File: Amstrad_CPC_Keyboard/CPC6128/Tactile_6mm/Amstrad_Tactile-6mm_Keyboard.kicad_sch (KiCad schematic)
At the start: 87 parts, among them J1 CP002, J3 CP001, J4 CP003, SW1 DEL (79), SW10 FOUR (56), SW11 THREE (57), SW12 E (58), SW13 W (59), SW14 S (60), SW15 D (61), SW16 C (62), SW17 X (63), SW18 SIX (48), SW19 FIVE (49), SW2 ONE (64), SW20 R (50), SW21 T (51), SW22 G (52), SW23 F (53), SW24 B (54), SW25 V (55), SW26 EIGHT (40), SW27 ZERO (32), SW28 ^CARAT^ (24), SW29 SEVEN (41), SW3 TWO (65), SW30 NINE (33), SW31 -MINUS- (25), SW32 U (42), SW33 O (34), SW34 @AT@ (26), SW35 Y (43), SW36 I (35), SW37 P (27), SW38 H (44), SW39 L (36), SW4 ESC (66), SW40 ;SEMI_COLON; (28), SW41 J (45), SW42 K (37), SW43 :COLON: (29), SW44 N (46), SW45 M (38), SW46 /FORWSLASH/ (30), SW47 SPACE (47), SW48 ,COMMA, (39), SW49 .DOT. (31), SW5 Q (67), SW50 CLR (16), SW51 LEFT (08), SW52 UP (00), SW53 [ (17), SW54 COPY (09), SW55 RIGHT (01), SW56 ENTER (18), SW57 ƒ7 (10), SW58 DOWN (02), SW59 ] (19), SW6 TAB (68), SW60 ƒ8 (11), SW61 ƒ9 (03), SW62 ƒ4 (20), SW63 ƒ5 (12), SW64 ƒ6 (04), SW65 LH_SHIFT (21), SW66 ƒ1 (13), SW67 ƒ3 (05), SW68 \BACKSLASH\ (22), SW69 ƒ2 (14), SW7 A (69), SW70 ENTER (06), SW71 CTRL (23), SW72 ƒ0 (15), SW73 .DOT. (07), SW74 RH_SHIFT (21), SW75 SW_SPDT, SW8 CAPS_LOCK (70), SW9 Z (71)

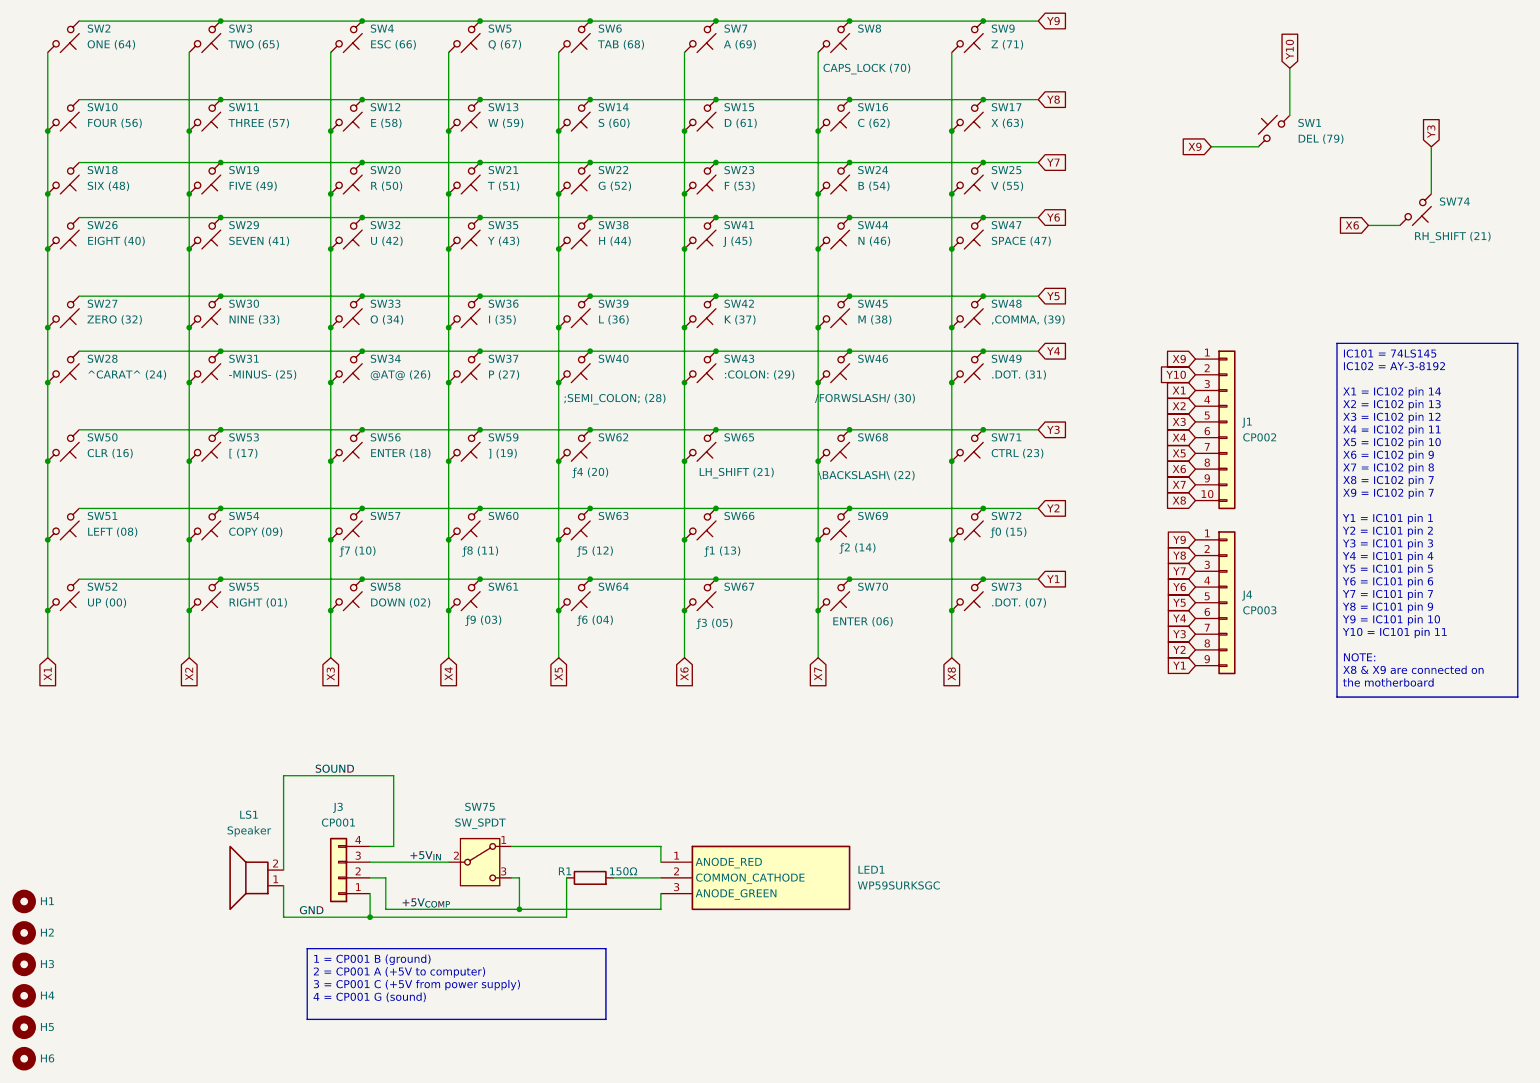
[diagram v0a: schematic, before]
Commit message: Added 6mm tactile design
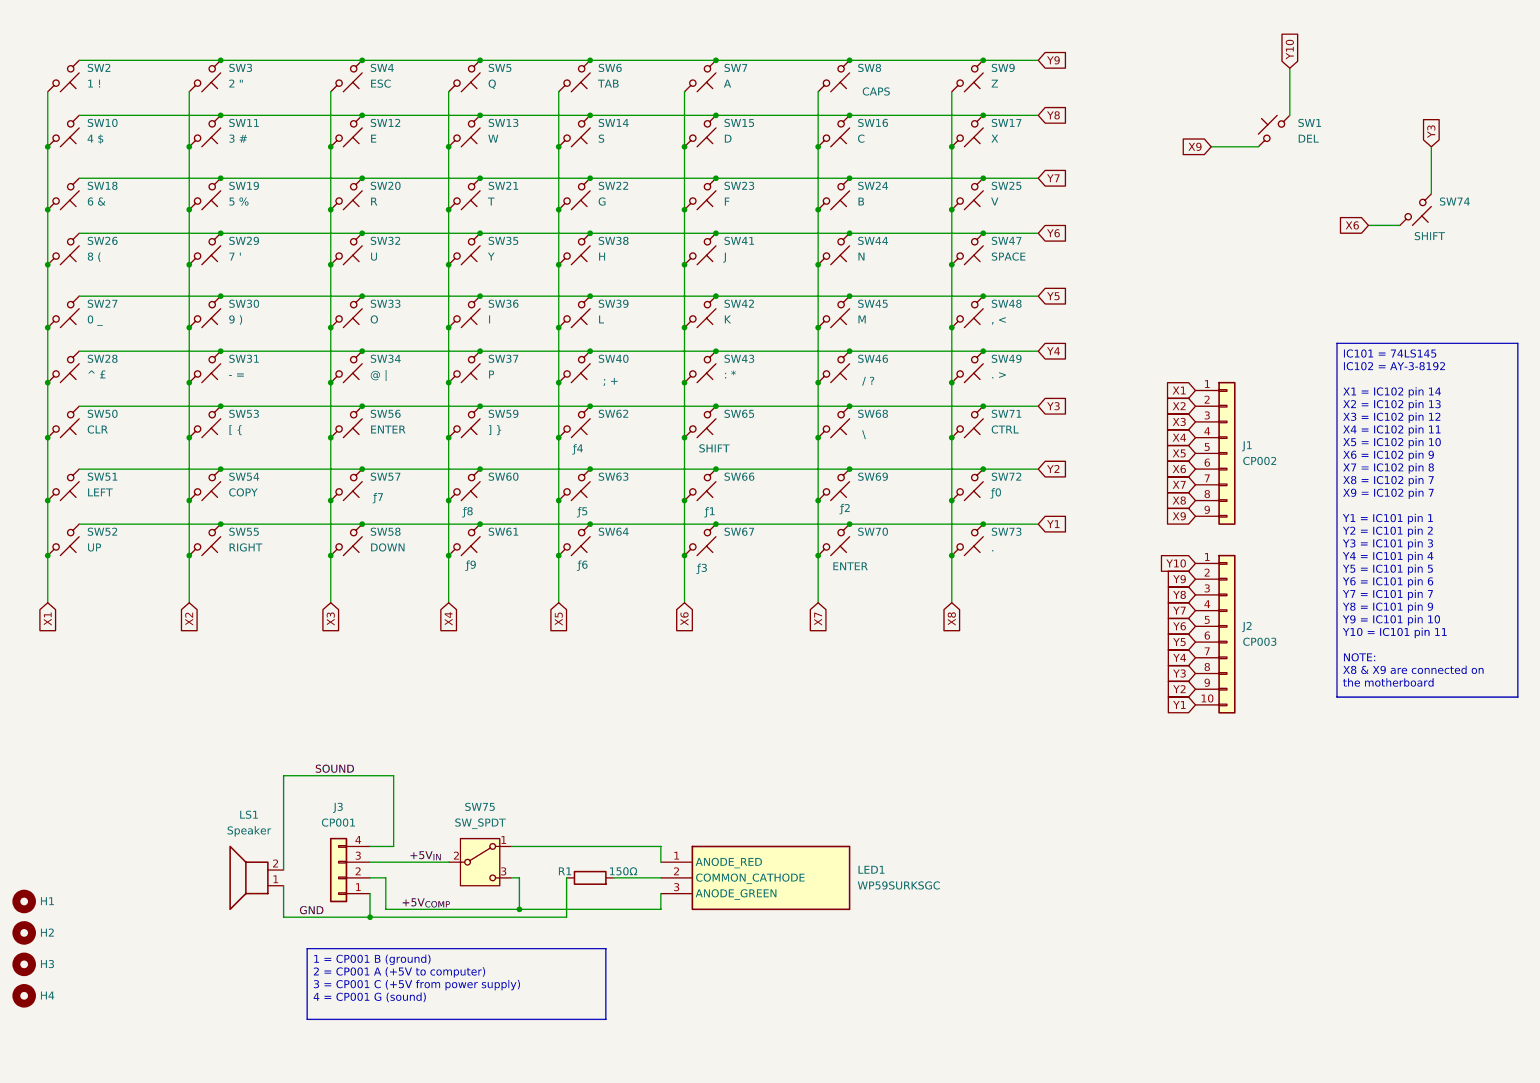
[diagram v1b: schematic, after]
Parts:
- removed H5, H6: MountingHole, MountingHole:MountingHole_3.2mm_M3, symbol Mechanical:MountingHole
- removed J1: CP002, Connector_PinHeader_2.54mm:PinHeader_1x10_P2.54mm_Vertical, symbol Connector_Generic:Conn_01x10
- removed J4: CP003, Connector_PinHeader_2.54mm:PinHeader_1x09_P2.54mm_Vertical, symbol Connector_Generic:Conn_01x09
- added J1: CP002, Connector_PinHeader_2.54mm:PinHeader_1x09_P2.54mm_Vertical, symbol Connector_Generic:Conn_01x09
- added J2: CP003, Connector_PinHeader_2.54mm:PinHeader_1x10_P2.54mm_Vertical, symbol Connector_Generic:Conn_01x10
- SW1: value DEL (79) -> DEL; footprint Button_Switch_THT:SW_PUSH-12mm -> Button_Switch_THT:SW_PUSH_6mm
- SW10: value FOUR (56) -> 4 $; footprint Button_Switch_THT:SW_PUSH-12mm -> Button_Switch_THT:SW_PUSH_6mm
- SW11: value THREE (57) -> 3 #; footprint Button_Switch_THT:SW_PUSH-12mm -> Button_Switch_THT:SW_PUSH_6mm
- SW12: value E (58) -> E; footprint Button_Switch_THT:SW_PUSH-12mm -> Button_Switch_THT:SW_PUSH_6mm
- SW13: value W (59) -> W; footprint Button_Switch_THT:SW_PUSH-12mm -> Button_Switch_THT:SW_PUSH_6mm
- SW14: value S (60) -> S; footprint Button_Switch_THT:SW_PUSH-12mm -> Button_Switch_THT:SW_PUSH_6mm
- SW15: value D (61) -> D; footprint Button_Switch_THT:SW_PUSH-12mm -> Button_Switch_THT:SW_PUSH_6mm
- SW16: value C (62) -> C; footprint Button_Switch_THT:SW_PUSH-12mm -> Button_Switch_THT:SW_PUSH_6mm
- SW17: value X (63) -> X; footprint Button_Switch_THT:SW_PUSH-12mm -> Button_Switch_THT:SW_PUSH_6mm
- SW18: value SIX (48) -> 6 &; footprint Button_Switch_THT:SW_PUSH-12mm -> Button_Switch_THT:SW_PUSH_6mm
- SW19: value FIVE (49) -> 5 %; footprint Button_Switch_THT:SW_PUSH-12mm -> Button_Switch_THT:SW_PUSH_6mm
- SW2: value ONE (64) -> 1 !; footprint Button_Switch_THT:SW_PUSH-12mm -> Button_Switch_THT:SW_PUSH_6mm
- SW20: value R (50) -> R; footprint Button_Switch_THT:SW_PUSH-12mm -> Button_Switch_THT:SW_PUSH_6mm
- SW21: value T (51) -> T; footprint Button_Switch_THT:SW_PUSH-12mm -> Button_Switch_THT:SW_PUSH_6mm
- SW22: value G (52) -> G; footprint Button_Switch_THT:SW_PUSH-12mm -> Button_Switch_THT:SW_PUSH_6mm
- SW23: value F (53) -> F; footprint Button_Switch_THT:SW_PUSH-12mm -> Button_Switch_THT:SW_PUSH_6mm
- SW24: value B (54) -> B; footprint Button_Switch_THT:SW_PUSH-12mm -> Button_Switch_THT:SW_PUSH_6mm
- SW25: value V (55) -> V; footprint Button_Switch_THT:SW_PUSH-12mm -> Button_Switch_THT:SW_PUSH_6mm
- SW26: value EIGHT (40) -> 8 (; footprint Button_Switch_THT:SW_PUSH-12mm -> Button_Switch_THT:SW_PUSH_6mm
- SW27: value ZERO (32) -> 0 _; footprint Button_Switch_THT:SW_PUSH-12mm -> Button_Switch_THT:SW_PUSH_6mm
- SW28: value ^CARAT^ (24) -> ^ £; footprint Button_Switch_THT:SW_PUSH-12mm -> Button_Switch_THT:SW_PUSH_6mm
- SW29: value SEVEN (41) -> 7 '; footprint Button_Switch_THT:SW_PUSH-12mm -> Button_Switch_THT:SW_PUSH_6mm
- SW3: value TWO (65) -> 2 "; footprint Button_Switch_THT:SW_PUSH-12mm -> Button_Switch_THT:SW_PUSH_6mm
- SW30: value NINE (33) -> 9 ); footprint Button_Switch_THT:SW_PUSH-12mm -> Button_Switch_THT:SW_PUSH_6mm
- SW31: value -MINUS- (25) -> - =; footprint Button_Switch_THT:SW_PUSH-12mm -> Button_Switch_THT:SW_PUSH_6mm
- SW32: value U (42) -> U; footprint Button_Switch_THT:SW_PUSH-12mm -> Button_Switch_THT:SW_PUSH_6mm
- SW33: value O (34) -> O; footprint Button_Switch_THT:SW_PUSH-12mm -> Button_Switch_THT:SW_PUSH_6mm
- SW34: value @AT@ (26) -> @ |; footprint Button_Switch_THT:SW_PUSH-12mm -> Button_Switch_THT:SW_PUSH_6mm
- SW35: value Y (43) -> Y; footprint Button_Switch_THT:SW_PUSH-12mm -> Button_Switch_THT:SW_PUSH_6mm
- SW36: value I (35) -> I; footprint Button_Switch_THT:SW_PUSH-12mm -> Button_Switch_THT:SW_PUSH_6mm
- SW37: value P (27) -> P; footprint Button_Switch_THT:SW_PUSH-12mm -> Button_Switch_THT:SW_PUSH_6mm
- SW38: value H (44) -> H; footprint Button_Switch_THT:SW_PUSH-12mm -> Button_Switch_THT:SW_PUSH_6mm
- SW39: value L (36) -> L; footprint Button_Switch_THT:SW_PUSH-12mm -> Button_Switch_THT:SW_PUSH_6mm
- SW4: value ESC (66) -> ESC; footprint Button_Switch_THT:SW_PUSH-12mm -> Button_Switch_THT:SW_PUSH_6mm
- SW40: value ;SEMI_COLON; (28) -> ; +; footprint Button_Switch_THT:SW_PUSH-12mm -> Button_Switch_THT:SW_PUSH_6mm
- SW41: value J (45) -> J; footprint Button_Switch_THT:SW_PUSH-12mm -> Button_Switch_THT:SW_PUSH_6mm
- SW42: value K (37) -> K; footprint Button_Switch_THT:SW_PUSH-12mm -> Button_Switch_THT:SW_PUSH_6mm
- SW43: value :COLON: (29) -> : *; footprint Button_Switch_THT:SW_PUSH-12mm -> Button_Switch_THT:SW_PUSH_6mm
- SW44: value N (46) -> N; footprint Button_Switch_THT:SW_PUSH-12mm -> Button_Switch_THT:SW_PUSH_6mm
- SW45: value M (38) -> M; footprint Button_Switch_THT:SW_PUSH-12mm -> Button_Switch_THT:SW_PUSH_6mm
- SW46: value /FORWSLASH/ (30) -> / ?; footprint Button_Switch_THT:SW_PUSH-12mm -> Button_Switch_THT:SW_PUSH_6mm
- SW47: value SPACE (47) -> SPACE; footprint Button_Switch_THT:SW_PUSH-12mm -> Button_Switch_THT:SW_PUSH_6mm
- SW48: value ,COMMA, (39) -> , <; footprint Button_Switch_THT:SW_PUSH-12mm -> Button_Switch_THT:SW_PUSH_6mm
- SW49: value .DOT. (31) -> . >; footprint Button_Switch_THT:SW_PUSH-12mm -> Button_Switch_THT:SW_PUSH_6mm
- SW5: value Q (67) -> Q; footprint Button_Switch_THT:SW_PUSH-12mm -> Button_Switch_THT:SW_PUSH_6mm
- SW50: value CLR (16) -> CLR; footprint Button_Switch_THT:SW_PUSH-12mm -> Button_Switch_THT:SW_PUSH_6mm
- SW51: value LEFT (08) -> LEFT; footprint Button_Switch_THT:SW_PUSH-12mm -> Button_Switch_THT:SW_PUSH_6mm
- SW52: value UP (00) -> UP; footprint Button_Switch_THT:SW_PUSH-12mm -> Button_Switch_THT:SW_PUSH_6mm
- SW53: value [ (17) -> [ {; footprint Button_Switch_THT:SW_PUSH-12mm -> Button_Switch_THT:SW_PUSH_6mm
- SW54: value COPY (09) -> COPY; footprint Button_Switch_THT:SW_PUSH-12mm -> Button_Switch_THT:SW_PUSH_6mm
- SW55: value RIGHT (01) -> RIGHT; footprint Button_Switch_THT:SW_PUSH-12mm -> Button_Switch_THT:SW_PUSH_6mm
- SW56: value ENTER (18) -> ENTER; footprint Button_Switch_THT:SW_PUSH-12mm -> Button_Switch_THT:SW_PUSH_6mm
- SW57: value ƒ7 (10) -> ƒ7; footprint Button_Switch_THT:SW_PUSH-12mm -> Button_Switch_THT:SW_PUSH_6mm
- SW58: value DOWN (02) -> DOWN; footprint Button_Switch_THT:SW_PUSH-12mm -> Button_Switch_THT:SW_PUSH_6mm
- SW59: value ] (19) -> ] }; footprint Button_Switch_THT:SW_PUSH-12mm -> Button_Switch_THT:SW_PUSH_6mm
- SW6: value TAB (68) -> TAB; footprint Button_Switch_THT:SW_PUSH-12mm -> Button_Switch_THT:SW_PUSH_6mm
- SW60: value ƒ8 (11) -> ƒ8; footprint Button_Switch_THT:SW_PUSH-12mm -> Button_Switch_THT:SW_PUSH_6mm
- SW61: value ƒ9 (03) -> ƒ9; footprint Button_Switch_THT:SW_PUSH-12mm -> Button_Switch_THT:SW_PUSH_6mm
- SW62: value ƒ4 (20) -> ƒ4; footprint Button_Switch_THT:SW_PUSH-12mm -> Button_Switch_THT:SW_PUSH_6mm
- SW63: value ƒ5 (12) -> ƒ5; footprint Button_Switch_THT:SW_PUSH-12mm -> Button_Switch_THT:SW_PUSH_6mm
- SW64: value ƒ6 (04) -> ƒ6; footprint Button_Switch_THT:SW_PUSH-12mm -> Button_Switch_THT:SW_PUSH_6mm
- SW65: value LH_SHIFT (21) -> SHIFT; footprint Button_Switch_THT:SW_PUSH-12mm -> Button_Switch_THT:SW_PUSH_6mm
- SW66: value ƒ1 (13) -> ƒ1; footprint Button_Switch_THT:SW_PUSH-12mm -> Button_Switch_THT:SW_PUSH_6mm
- SW67: value ƒ3 (05) -> ƒ3; footprint Button_Switch_THT:SW_PUSH-12mm -> Button_Switch_THT:SW_PUSH_6mm
- SW68: value \BACKSLASH\ (22) -> \; footprint Button_Switch_THT:SW_PUSH-12mm -> Button_Switch_THT:SW_PUSH_6mm
- SW69: value ƒ2 (14) -> ƒ2; footprint Button_Switch_THT:SW_PUSH-12mm -> Button_Switch_THT:SW_PUSH_6mm
- SW7: value A (69) -> A; footprint Button_Switch_THT:SW_PUSH-12mm -> Button_Switch_THT:SW_PUSH_6mm
- SW70: value ENTER (06) -> ENTER; footprint Button_Switch_THT:SW_PUSH-12mm -> Button_Switch_THT:SW_PUSH_6mm
- SW71: value CTRL (23) -> CTRL; footprint Button_Switch_THT:SW_PUSH-12mm -> Button_Switch_THT:SW_PUSH_6mm
- SW72: value ƒ0 (15) -> ƒ0; footprint Button_Switch_THT:SW_PUSH-12mm -> Button_Switch_THT:SW_PUSH_6mm
- SW73: value .DOT. (07) -> .; footprint Button_Switch_THT:SW_PUSH-12mm -> Button_Switch_THT:SW_PUSH_6mm
- SW74: value RH_SHIFT (21) -> SHIFT; footprint Button_Switch_THT:SW_PUSH-12mm -> Button_Switch_THT:SW_PUSH_6mm
- SW8: value CAPS_LOCK (70) -> CAPS; footprint Button_Switch_THT:SW_PUSH-12mm -> Button_Switch_THT:SW_PUSH_6mm
- SW9: value Z (71) -> Z; footprint Button_Switch_THT:SW_PUSH-12mm -> Button_Switch_THT:SW_PUSH_6mm
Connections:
- net X1: now also J1.1 (Pin_1)
- net X2: now also J1.2 (Pin_2)
- net X3: now also J1.3 (Pin_3)
- net X4: now also J1.4 (Pin_4)
- net X5: now also J1.5 (Pin_5)
- net X6: now also J1.6 (Pin_6)
- net X7: now also J1.7 (Pin_7)
- net X8: now also J1.8 (Pin_8)
- net X9: now also J1.9 (Pin_9)
- net Y1: now also J2.10 (Pin_10)
- net Y10: now also J2.1 (Pin_1)
- net Y2: now also J2.9 (Pin_9)
- net Y3: now also J2.8 (Pin_8)
- net Y4: now also J2.7 (Pin_7)
- net Y5: now also J2.6 (Pin_6)
- net Y6: now also J2.5 (Pin_5)
- net Y7: now also J2.4 (Pin_4)
- net Y8: now also J2.3 (Pin_3)
- net Y9: now also J2.2 (Pin_2)
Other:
- moved on the sheet: SW10, SW11, SW12, SW13, SW14, SW15, SW16, SW17, SW18, SW19, SW2, SW20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
